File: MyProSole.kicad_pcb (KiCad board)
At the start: 2 copper layers, 22 parts, among them J1 FSR3, J2 FSR2, J3 FSR3, J4 Conn_01x07_Socket_XIAO_ESP32C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, J5 i2c-bus, J6 SD_CardSocket, J7 XIAO_ESP32C3, J8 SD_CardSocketDummy

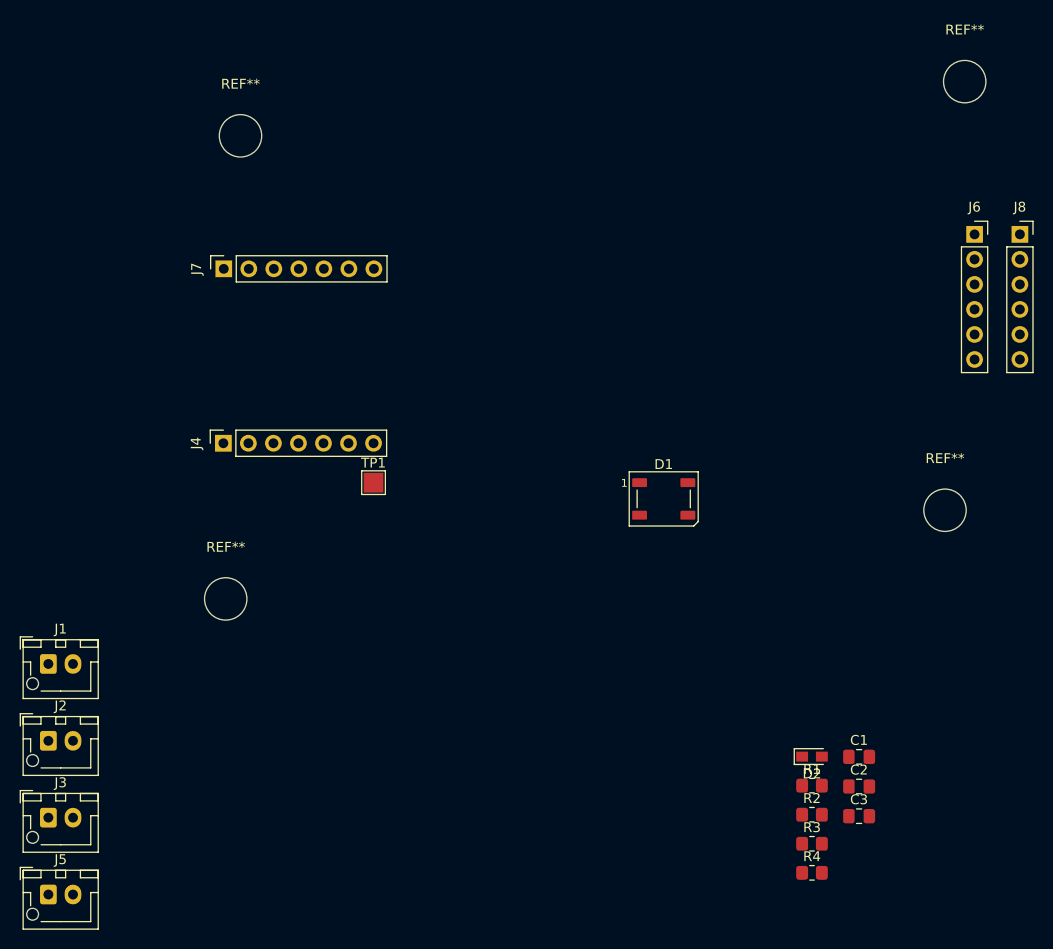
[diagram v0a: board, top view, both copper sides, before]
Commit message: First Step for Layout
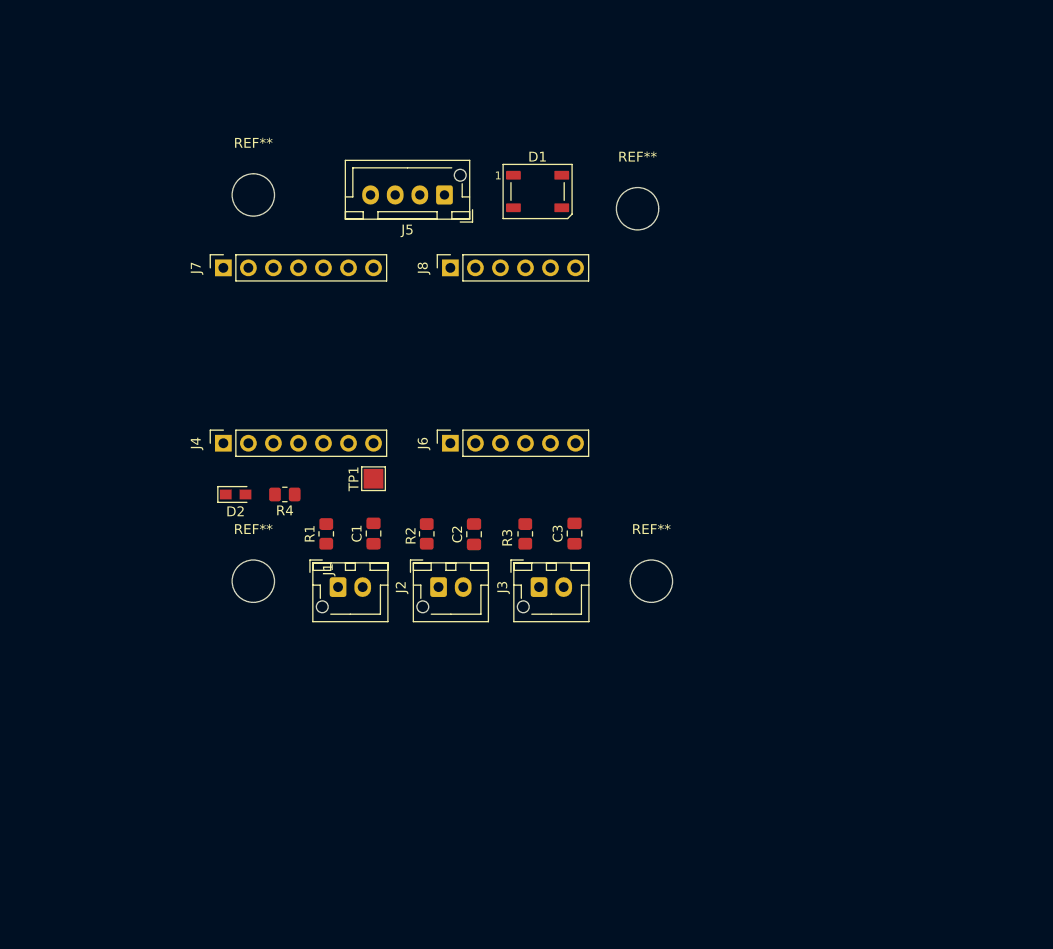
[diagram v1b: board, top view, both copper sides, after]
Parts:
- J5: footprint Connector_JST:JST_XH_B2B-XH-AM_1x02_P2.50mm_Vertical -> Connector_JST:JST_XH_B4B-XH-AM_1x04_P2.50mm_Vertical
- moved J5 81.6 mm to (101.2, 50.0), turned to 180 degrees
- moved R4 65.9 mm to (85.0, 80.4), turned to 180 degrees
- moved D2 64.3 mm to (80.0, 80.4)
- moved J8 57.9 mm to (101.8, 57.4), turned to 90 degrees
- moved J6 57.3 mm to (101.8, 75.2), turned to 90 degrees
- moved R1 55.5 mm to (89.2, 84.4), turned to 90 degrees
- moved J3 55.0 mm to (110.8, 89.8)
- moved C1 54.2 mm to (94.0, 84.4), turned to 90 degrees
- moved R2 48.4 mm to (99.4, 84.4), turned to 90 degrees
- moved C2 46.7 mm to (104.2, 84.4), turned to 90 degrees
- moved R3 42.8 mm to (109.4, 84.4), turned to 90 degrees
- moved J2 42.6 mm to (100.6, 89.8)
- moved C3 40.7 mm to (114.4, 84.4), turned to 90 degrees
- moved REF** 35.6 mm to (120.8, 51.4)
- moved D1 33.7 mm to (110.7, 49.6)
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
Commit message: New arragement
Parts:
- moved J5 41.2 mm to (121.4, 85.9), turned to 90 degrees
- moved TP1 28.3 mm to (91.5, 50.6)
- moved J6 18.3 mm to (120.0, 72.5)
- moved J8 18.3 mm to (120.0, 57.4)
- moved D1 10.0 mm to (120.5, 51.4)
- moved REF** 9.49 mm to (130.2, 50.5)
- moved REF** 9.17 mm to (130.1, 84.5)
- moved C2 6.35 mm to (102.8, 78.2)
- moved C3 6.35 mm to (113.0, 78.2)
- moved R1 6.35 mm to (87.8, 78.2)
- moved R2 6.35 mm to (98.0, 78.2)
- moved R3 6.35 mm to (108.0, 78.2)
- moved C1 6.35 mm to (92.7, 78.2)
- moved J1 5.23 mm to (89.0, 84.8)
- moved J2 5.23 mm to (99.2, 84.8)
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
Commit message: almost ready for review
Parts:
- moved TP1 19.2 mm to (96.8, 69.0), turned to 180 degrees
- moved J7 15.2 mm to (94.0, 57.5), turned to -90 degrees
- moved D2 5.00 mm to (84.0, 77.2), turned to 180 degrees
- moved R4 5.00 mm to (79.0, 77.2), turned to 0 degrees
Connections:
- J1 pad 2: GND -> +3.3V
- J2 pad 2: GND -> +3.3V
- J3 pad 2: GND -> +3.3V
- J5 pad 2: /SCL -> /SDA
- J5 pad 3: /SDA -> /SCL
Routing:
- net +3.3V: track 0.00 -> 143.4 mm
- net /RGB_LED: track 0.00 -> 57.3 mm
- net /CS: track 0.00 -> 45.1 mm
- net /SCK: track 0.00 -> 44.9 mm
- net /MOSI: track 0.00 -> 44.9 mm
- net /MISO: track 0.00 -> 44.9 mm
- net /FSR3_Input: track 0.00 -> 41.7 mm
- net /SDA: track 0.00 -> 36.9 mm
- net /FSR2_Input: track 0.00 -> 33.9 mm
- net /SCL: track 0.00 -> 33.4 mm
- net /FSR1_Input: track 0.00 -> 26.2 mm
- net +5V: track 0.00 -> 21.0 mm
- net Net-(J4-GPIO_21): track 0.00 -> 4.71 mm
- net Net-(D2-A): track 0.00 -> 3.00 mm
- added copper zone on B.Cu, net GND
- added copper zone on F.Cu, net GND
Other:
- board outline added: 58.9 x 43.6 mm
- board text added: "Batterie"

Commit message: Versoin bevor review
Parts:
- J1: value FSR3 -> FSR1
- J5: value i2c-bus -> i²c / gyroscope
- moved TP1 1.60 mm to (95.2, 69.0)
- moved D2 0.81 mm to (83.5, 77.8), turned to 0 degrees
- moved R4 0.06 mm to (78.9, 77.2), turned to 90 degrees
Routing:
- net GND: track 0.00 -> 34.7 mm, vias 0 -> 7
- net Net-(D2-A): track 3.00 -> 6.88 mm
- net +5V: track 21.0 -> 21.9 mm
- net Net-(J4-GPIO_21): track 4.71 -> 4.05 mm
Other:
- board text added: "100nF"
- board text added: "USB"

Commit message: Added Revisoin Version & Date on Backplate
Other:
- board text added: "MyProSole Rev ${Revision} - ${Date}"
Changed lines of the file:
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@@
+		)
+	)
+	(gr_text "MyProSole Rev ${Revision}  -  ${Date}"
+		(at 120.8 48.8 0)
+		(layer "B.SilkS")
+		(effects
+			(font
+				(size 1 1)
+				(thickness 0.1)
+			)
+			(justify left bottom mirror)
 		)
 	)

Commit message: first prototyp versions
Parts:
- added C4: 10uF, Capacitor_SMD:C_0805_2012Metric_Pad1.18x1.45mm_HandSolder, F.Cu at (82.4, 60.6)
- added D3: ESD5Zxx, Diode_SMD:D_SOD-523, F.Cu at (89.7, 81.2)
- added D4: ESD5Zxx, Diode_SMD:D_SOD-523, F.Cu at (99.8, 81.2)
- added D5: ESD5Zxx, Diode_SMD:D_SOD-523, F.Cu at (110.0, 81.2)
- C1, C2, C3: value 100nF -> 10nF
- D2: value 5V Power LED -> USB-LED
- J1: value FSR1 -> FSR3
- J5: value i²c / gyroscope -> i2c-bus
- moved C1 0.92 mm to (91.8, 78.5)
- moved C3 0.91 mm to (112.2, 78.5)
- moved C2 0.87 mm to (102.0, 78.4)
- moved R2 0.53 mm to (97.6, 78.5)
- moved R1 0.37 mm to (87.6, 78.5)
- moved R3 0.37 mm to (107.8, 78.5)
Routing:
- net +3.3V: track 143.4 -> 146.7 mm
- net /FSR3_Input: track 41.7 -> 40.4 mm
- net /FSR2_Input: track 33.9 -> 32.7 mm
- net /FSR1_Input: track 26.2 -> 25.1 mm
- net GND: track 34.7 -> 35.7 mm, vias 7 -> 14
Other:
- board text added: "V1.0 BG/2025-12"
- board text removed: "100nF"
- board text removed: "MyProSole Rev ${Revision} - ${Date}"

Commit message: Added ESP Step
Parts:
- added REF**: Unbenannt, MyProSoleLib:Unbenannt, F.Cu at (81.6, 67.5)
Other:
- board text added: "MyProSole V1.01 BG/2026-01"
- board text removed: "V1.0 BG/2025-12"
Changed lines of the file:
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@@
+		)
+	)
+	(footprint "MyProSoleLib:Unbenannt"
+		(layer "F.Cu")
+		(at 81.6 67.5 180)
+		(property "Reference" "REF**"
+			(at 0 -0.5 180)
+			(unlocked yes)
+			(layer "F.SilkS")
+			(effects
+				(font
+					(size 1 1)
+					(thickness 0.1)
+				)
+			)
+		)
+		(property "Value" "Unbenannt"
+			(at 0 1 180)
+			(unlocked yes)
+			(layer "F.Fab")
+			(effects
+				(font
+					(size 1 1)
+					(thickness 0.15)
+				)
+			)
+		)
+		(property "Datasheet" ""
+			(at 0 0 180)
+			(unlocked yes)
+			(layer "F.Fab")
+			(hide yes)
+			(effects
+				(font
+					(size 1 1)
+					(thickness 0.15)
+				)
+			)
+		)
+		(property "Description" ""
+			(at 0 0 180)
+			(unlocked yes)
+			(layer "F.Fab")
+			(hide yes)
+			(effects
+				(font
+					(size 1 1)
+					(thickness 0.15)
+				)
+			)
+		)
+		(attr smd)
+		(fp_rect
+			(start -15.5 -6.5)
+			(end 5.5 11.5)
+			(stroke
+				(width 0.1)
+				(type default)
+			)
+			(fill no)
+			(layer "F.SilkS")
+		)
+		(fp_text user "${REFERENCE}"
+			(at 0 2.5 180)
+			(unlocked yes)
+			(layer "F.Fab")
+			(effects
+				(font
+					(size 1 1)
+					(thickness 0.15)
+				)
+			)
+		)
+		(embedded_fonts no)
+		(model "/home/bgores/Dokumente/seeed-studio-xiao-esp32-c6-1.snapshot.3/Seeed Studio XIAO ESP32-C6.step"
+			(offset
+				(xyz -7 -8.5 0)
+			)
+			(scale
+				(xyz 1 1 1)
+			)
+			(rotate
+				(xyz -90 -0 -0)
+			)
 		)
 	)
@@
 	)
 	(gr_text "Batterie"
-		(at 84.345 39.9 0)
+		(at 103.6 58.8 0)
 		(layer "F.SilkS")
 		(effects
@@
 		)
 	)
-	(gr_text "V1.0\nBG/2025-12"
-		(at 109.8 68.6 0)
+	(gr_text "MyProSole V1.01\nBG/2026-01"
+		(at 124 69.4 0)
 		(layer "B.SilkS")
 		(effects
 			(font
-				(size 1 1)
-				(thickness 0.1)
+				(size 2 2)
+				(thickness 0.5)
+				(bold yes)
 			)
 			(justify left bottom mirror)

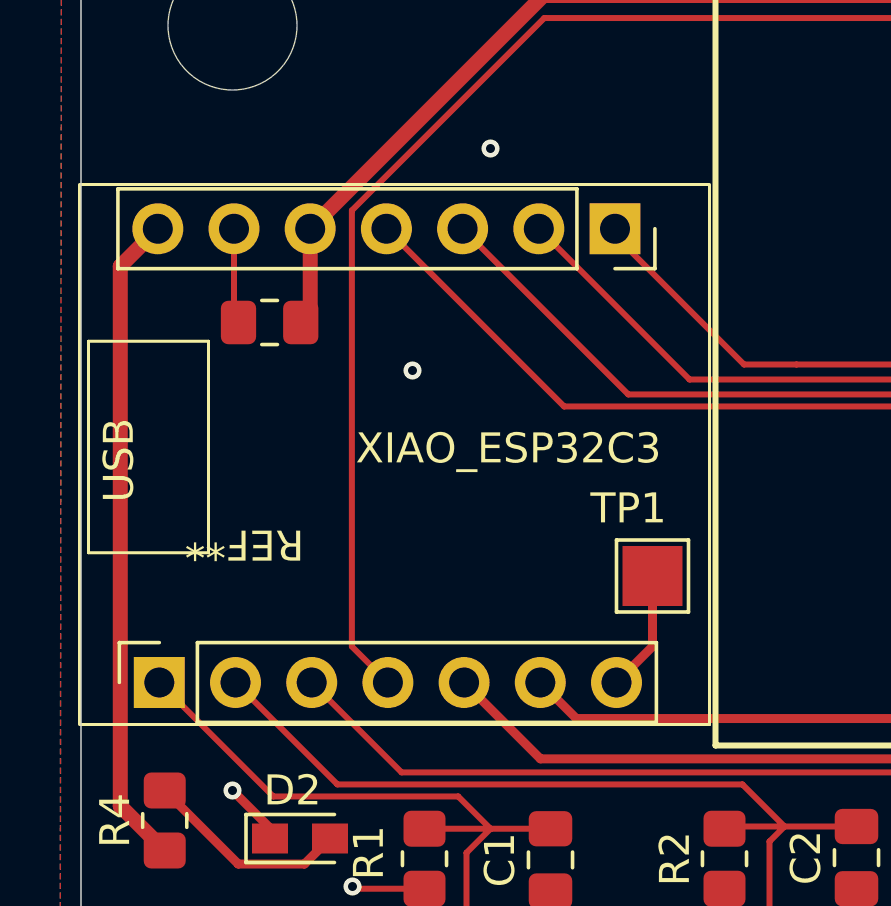
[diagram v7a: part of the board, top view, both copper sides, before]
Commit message: Fixed ESP32_C3 3D Model
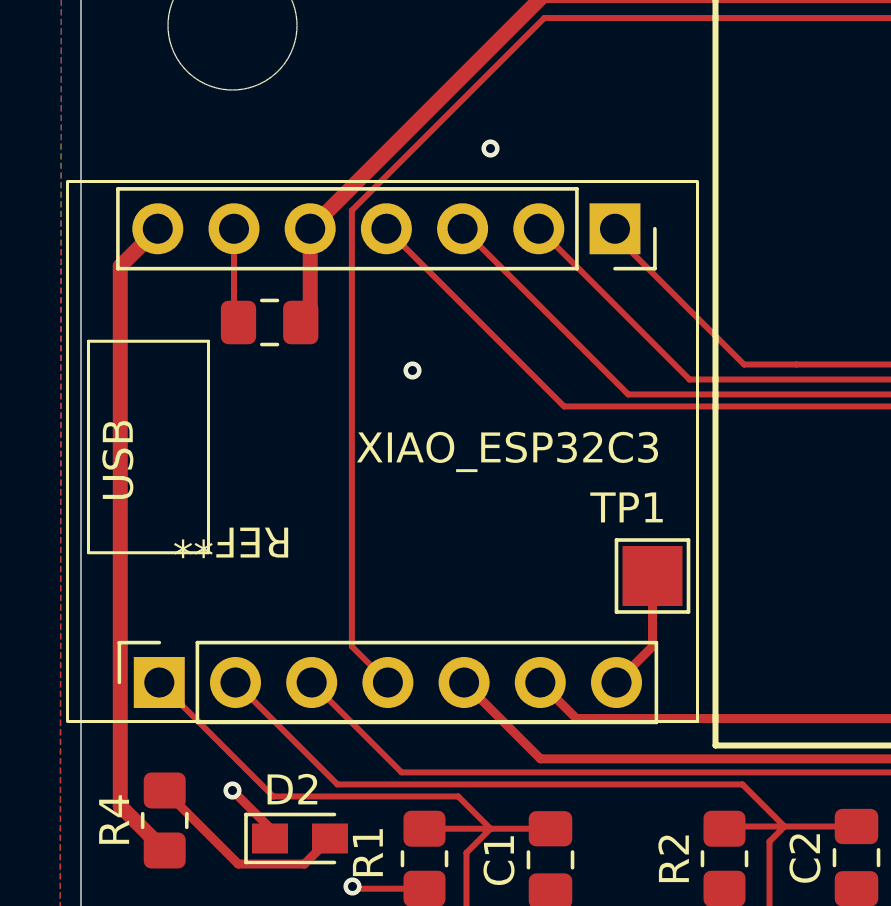
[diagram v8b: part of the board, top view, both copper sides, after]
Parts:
- removed the REF** at (81.6, 67.5)
- added REF**: ESP32_C3, MyProSoleLib:ESP32_C3, F.Cu at (81.2, 67.4)
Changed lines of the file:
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@@
 		(embedded_fonts no)
+	)
+	(footprint "MyProSoleLib:ESP32_C3"
+		(layer "F.Cu")
+		(at 81.2 67.4 180)
+		(property "Reference" "REF**"
+			(at 0 -0.5 180)
+			(unlocked yes)
+			(layer "F.SilkS")
+			(effects
+				(font
+					(size 1 1)
+					(thickness 0.1)
+				)
+			)
+		)
+		(property "Value" "ESP32_C3"
+			(at 0 1 180)
+			(unlocked yes)
+			(layer "F.Fab")
+			(effects
+				(font
+					(size 1 1)
+					(thickness 0.15)
+				)
+			)
+		)
+		(property "Datasheet" ""
+			(at 0 0 180)
+			(unlocked yes)
+			(layer "F.Fab")
+			(hide yes)
+			(effects
+				(font
+					(size 1 1)
+					(thickness 0.15)
+				)
+			)
+		)
+		(property "Description" ""
+			(at 0 0 180)
+			(unlocked yes)
+			(layer "F.Fab")
+			(hide yes)
+			(effects
+				(font
+					(size 1 1)
+					(thickness 0.15)
+				)
+			)
+		)
+		(attr smd)
+		(fp_rect
+			(start -15.5 -6.5)
+			(end 5.5 11.5)
+			(stroke
+				(width 0.1)
+				(type default)
+			)
+			(fill no)
+			(layer "F.SilkS")
+		)
+		(fp_text user "${REFERENCE}"
+			(at 0 2.5 180)
+			(unlocked yes)
+			(layer "F.Fab")
+			(effects
+				(font
+					(size 1 1)
+					(thickness 0.15)
+				)
+			)
+		)
+		(embedded_fonts no)
+		(model "/home/bgores/Dokumente/seeed-studio-xiao-esp32-c6-1.snapshot.3/Seeed Studio XIAO ESP32-C6.step"
+			(offset
+				(xyz -7 -8.5 7)
+			)
+			(scale
+				(xyz 1 1 1)
+			)
+			(rotate
+				(xyz -90 -0 -0)
+			)
+		)
 	)
 	(footprint "Diode_SMD:D_SOD-523"
@@
 			)
 		)
-	)
-	(footprint "MyProSoleLib:Unbenannt"
-		(layer "F.Cu")
-		(at 81.6 67.5 180)
-		(property "Reference" "REF**"
-			(at 0 -0.5 180)
-			(unlocked yes)
-			(layer "F.SilkS")
-			(effects
-				(font
-					(size 1 1)
-					(thickness 0.1)
-				)
-			)
-		)
-		(property "Value" "Unbenannt"
-			(at 0 1 180)
-			(unlocked yes)
-			(layer "F.Fab")
-			(effects
-				(font
-					(size 1 1)
-					(thickness 0.15)
-				)
-			)
-		)
-		(property "Datasheet" ""
-			(at 0 0 180)
-			(unlocked yes)
-			(layer "F.Fab")
-			(hide yes)
-			(effects
-				(font
-					(size 1 1)
-					(thickness 0.15)
-				)
-			)
-		)
-		(property "Description" ""
-			(at 0 0 180)
-			(unlocked yes)
-			(layer "F.Fab")
-			(hide yes)
-			(effects
-				(font
-					(size 1 1)
-					(thickness 0.15)
-				)
-			)
-		)
-		(attr smd)
-		(fp_rect
-			(start -15.5 -6.5)
-			(end 5.5 11.5)
-			(stroke
-				(width 0.1)
-				(type default)
-			)
-			(fill no)
-			(layer "F.SilkS")
-		)
-		(fp_text user "${REFERENCE}"
-			(at 0 2.5 180)
-			(unlocked yes)
-			(layer "F.Fab")
-			(effects
-				(font
-					(size 1 1)
-					(thickness 0.15)
-				)
-			)
-		)
-		(embedded_fonts no)
-		(model "/home/bgores/Dokumente/seeed-studio-xiao-esp32-c6-1.snapshot.3/Seeed Studio XIAO ESP32-C6.step"
-			(offset
-				(xyz -7 -8.5 0)
-			)
-			(scale
-				(xyz 1 1 1)
-			)
-			(rotate
-				(xyz -90 -0 -0)
-			)
-		)
